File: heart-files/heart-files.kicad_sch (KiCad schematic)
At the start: 31 parts, among them SW10 SW_Push, SW11 SW_Push, SW12 SW_Push, SW13 SW_Push, SW14 SW_Push, SW15 SW_Push, SW16 SW_Push, SW2 SW_Push, SW3 SW_Push, SW4 SW_Push, SW5 SW_Push, SW6 SW_Push, SW7 SW_Push, SW8 SW_Push, SW9 SW_Push

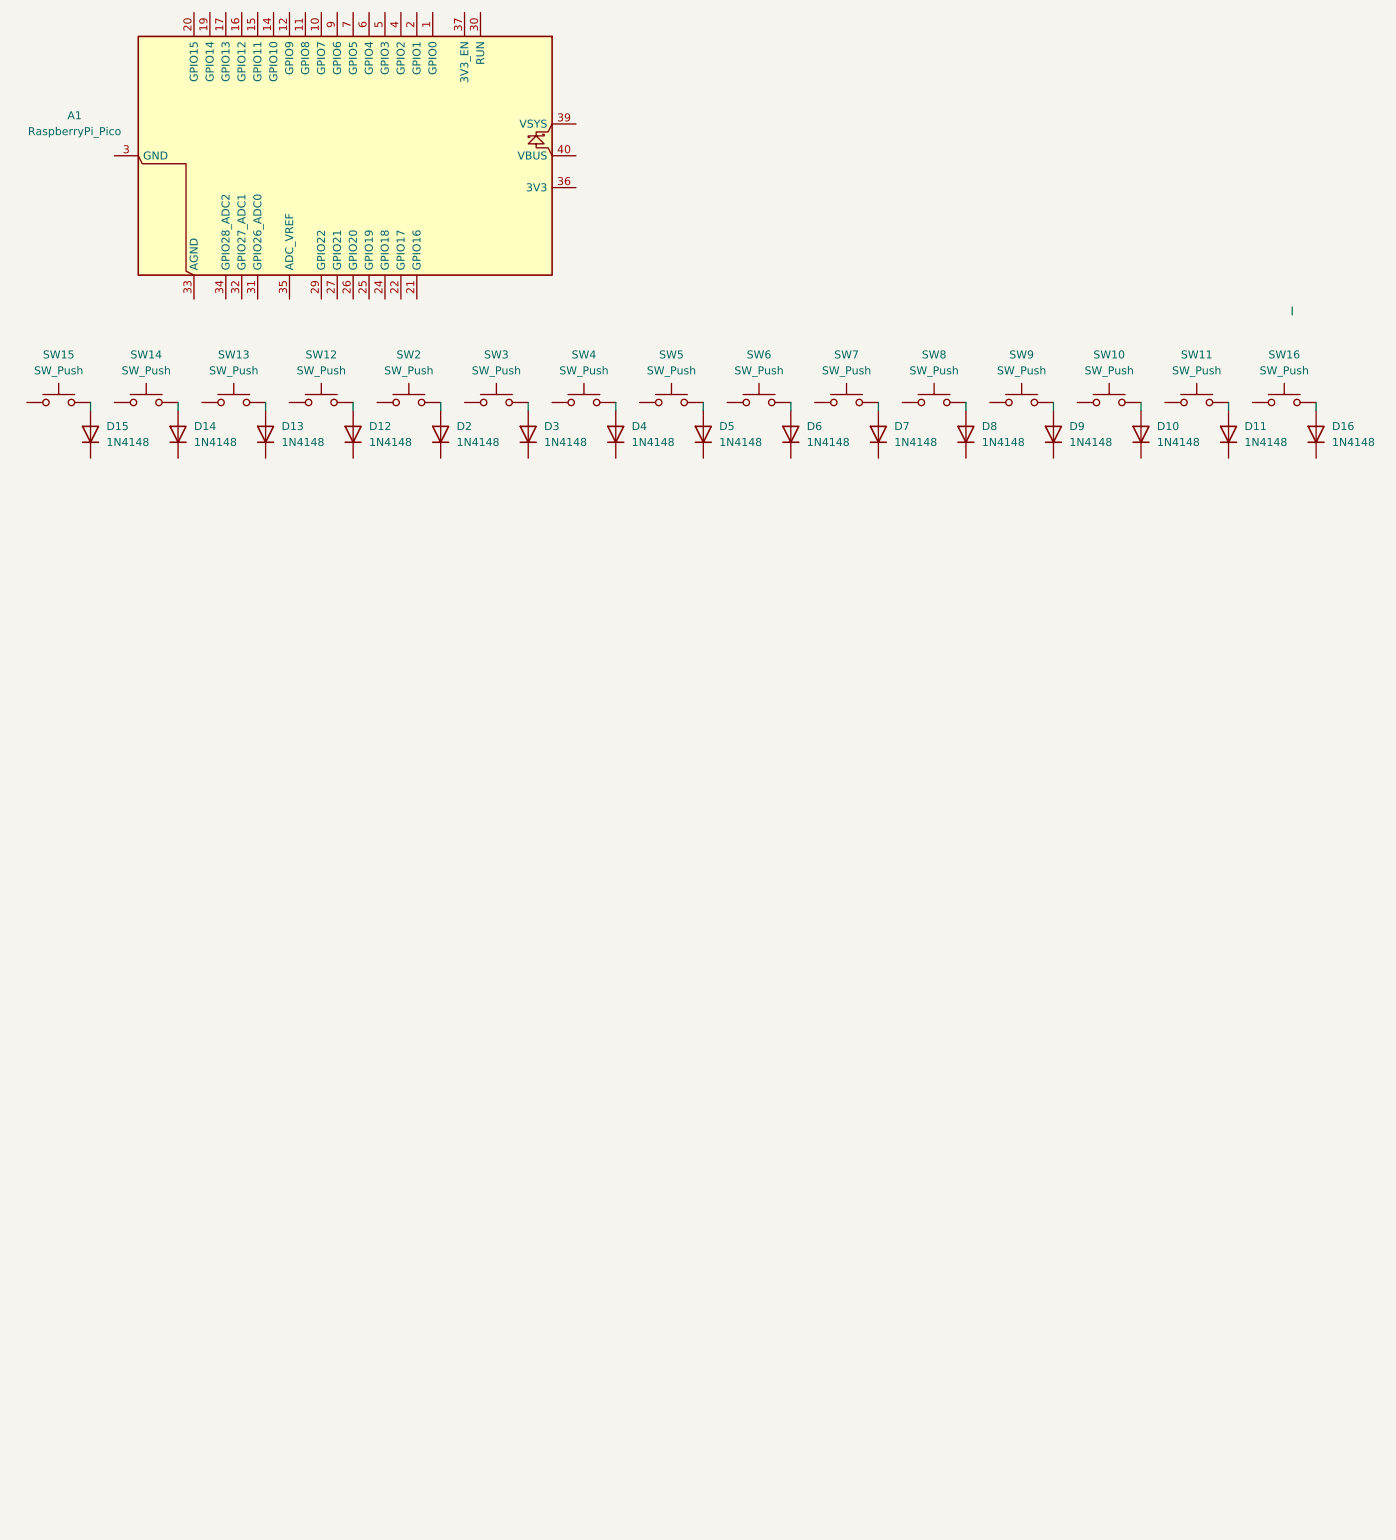
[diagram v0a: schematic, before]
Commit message: update readme and develop pcb, init bom(b)
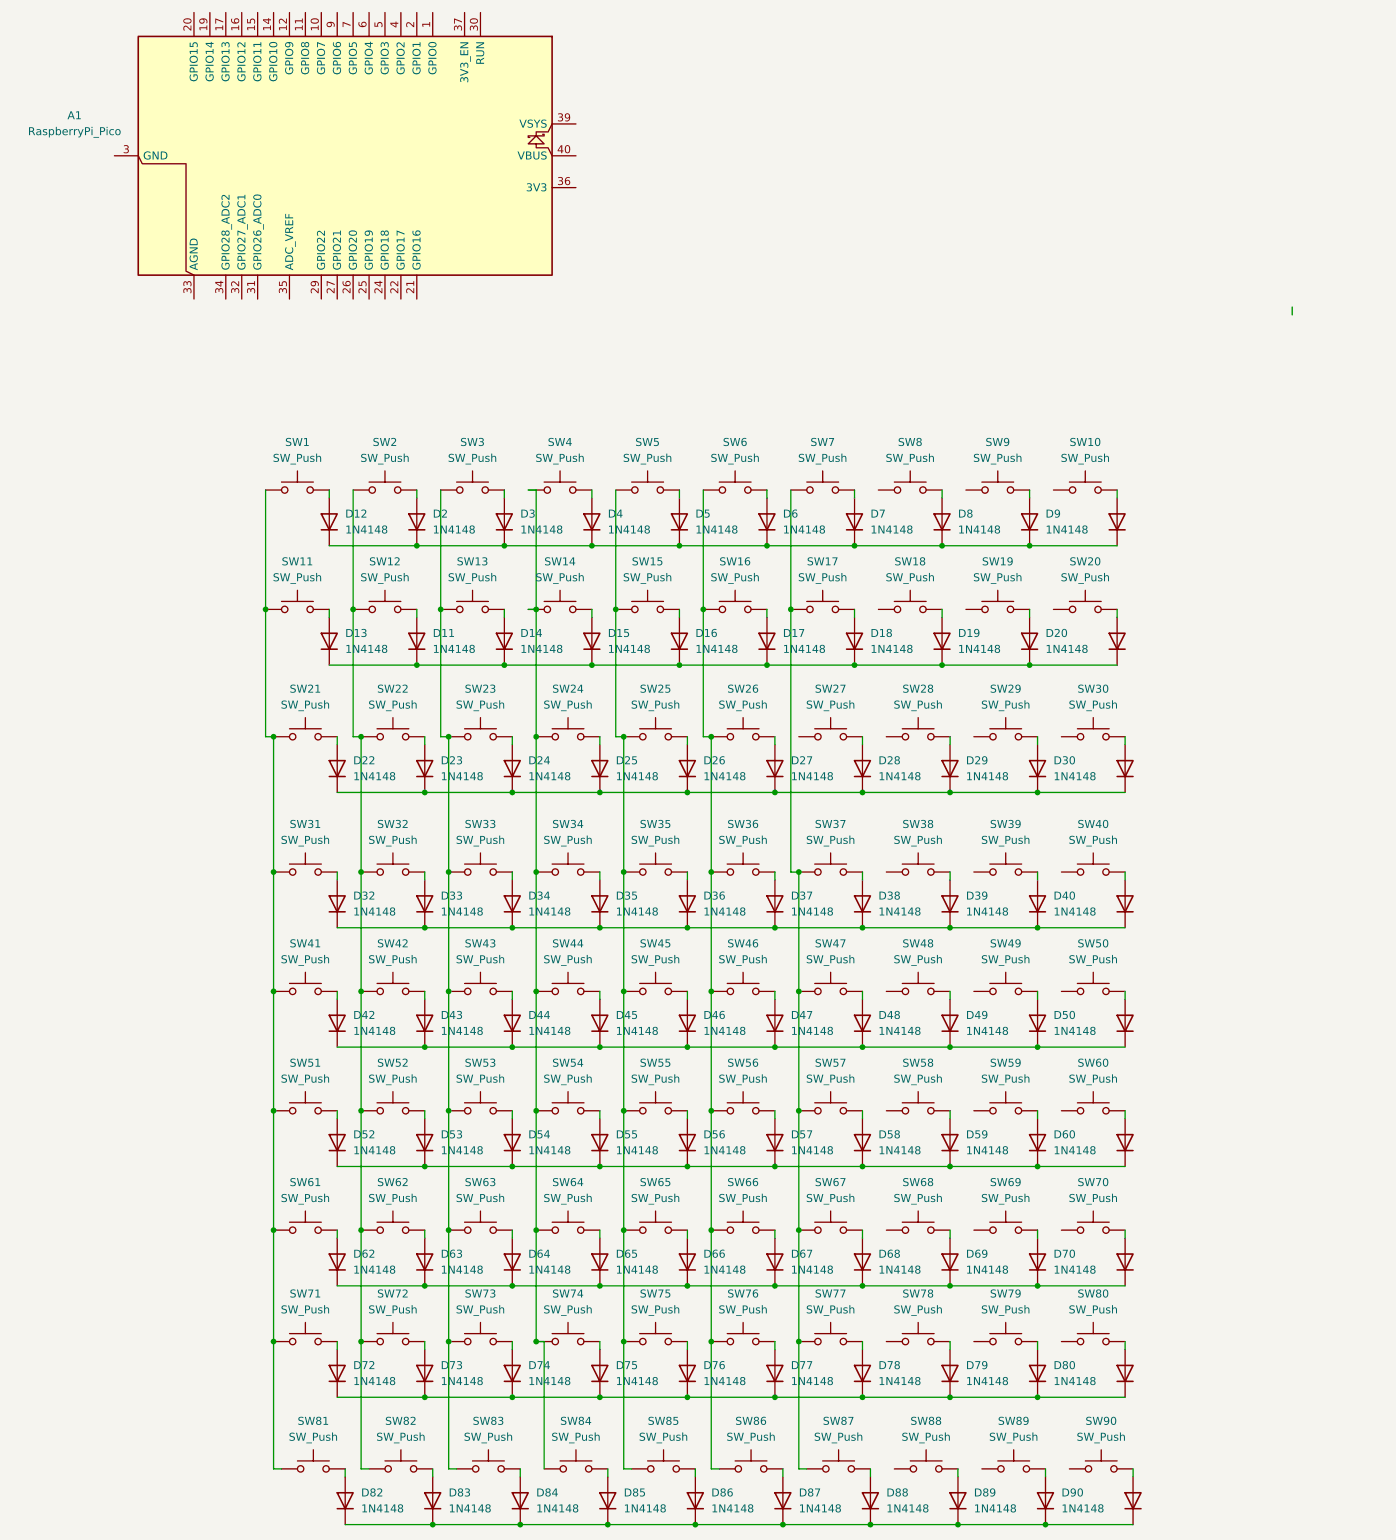
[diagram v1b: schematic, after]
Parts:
- added D17, D18, D19, D20, D21, D22, D23, D24, D25, D26, D27, D28, D29, D30, D31, D32, D33, D34, D35, D36, D37, D38, D39, D40, D41, D42, D43, D44, D45, D46, D47, D48, D49, D50, D51, D52, D53, D54, D55, D56, D57, D58, D59, D60, D61, D62, D63, D64, D65, D66, D67, D68, D69, D70, D71, D72, D73, D74, D75, D76, D77, D78, D79, D80, D81, D82, D83, D84, D85, D86, D87, D88, D89, D90, D91: 1N4148, Diode_THT:D_DO-35_SOD27_P7.62mm_Horizontal, symbol Diode:1N4148
- added SW12, SW17, SW18, SW19, SW20, SW21, SW22, SW23, SW24, SW25, SW26, SW27, SW28, SW29, SW30, SW31, SW32, SW33, SW34, SW35, SW36, SW37, SW38, SW39, SW40, SW41, SW42, SW43, SW44, SW45, SW46, SW47, SW48, SW49, SW50, SW51, SW52, SW53, SW54, SW55, SW56, SW57, SW58, SW59, SW60, SW61, SW62, SW63, SW64, SW65, SW66, SW67, SW68, SW69, SW70, SW71, SW72, SW73, SW74, SW75, SW76, SW77, SW78, SW79, SW80, SW81, SW82, SW83, SW84, SW85, SW86, SW87, SW88, SW89, SW90: SW_Push, symbol Switch:SW_Push
- renumbered SW12 to SW1
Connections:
- net at D10.1 (K): now also D12.1 (K), D2.1 (K), D3.1 (K), D4.1 (K), D5.1 (K), D6.1 (K), D7.1 (K), D8.1 (K), D9.1 (K)
- net at D11.1 (K): now also D13.1 (K), D14.1 (K), D15.1 (K), D16.1 (K), D17.1 (K), D18.1 (K), D19.1 (K), D20.1 (K), D21.1 (K)
- net at D11.2 (A): now also SW12.2; no longer SW11.2
- net at SW3.1: now also SW13.1, SW23.1, SW33.1, SW43.1, SW53.1, SW63.1, SW73.1, SW83.1
- net at SW14.1: now also SW4.1, SW24.1, SW34.1, SW44.1, SW54.1, SW64.1, SW74.1, SW84.1
- net at SW14.2: now also D15.2 (A); no longer D14.2 (A)
- net at D13.2 (A): now also SW11.2; no longer SW13.2
- net at D16.2 (A): now also SW15.2; no longer SW16.2
- net at SW11.1: now also SW1.1, SW21.1, SW31.1, SW41.1, SW51.1, SW61.1, SW71.1, SW81.1
- net at SW6.1: now also SW16.1, SW26.1, SW36.1, SW46.1, SW56.1, SW66.1, SW76.1, SW86.1
- net at SW2.1: now also SW12.1, SW22.1, SW32.1, SW42.1, SW52.1, SW62.1, SW72.1, SW82.1
- net at SW15.1: now also SW5.1, SW25.1, SW35.1, SW45.1, SW55.1, SW65.1, SW75.1, SW85.1
- net at SW7.1: now also SW17.1, SW37.1, SW47.1, SW57.1, SW67.1, SW77.1, SW87.1
- new net: D52.1 (K), D53.1 (K), D54.1 (K), D55.1 (K), D56.1 (K), D57.1 (K), D58.1 (K), D59.1 (K), D60.1 (K), D61.1 (K)
- new net: D60.2 (A), SW59.2
- new net: D32.1 (K), D33.1 (K), D34.1 (K), D35.1 (K), D36.1 (K), D37.1 (K), D38.1 (K), D39.1 (K), D40.1 (K), D41.1 (K)
- new net: D32.2 (A), SW31.2
- new net: D53.2 (A), SW52.2
- new net: D50.2 (A), SW49.2
- new net: D42.1 (K), D43.1 (K), D44.1 (K), D45.1 (K), D46.1 (K), D47.1 (K), D48.1 (K), D49.1 (K), D50.1 (K), D51.1 (K)
- new net: D45.2 (A), SW44.2
- new net: D74.2 (A), SW73.2
- new net: D82.2 (A), SW81.2
- new net: D25.2 (A), SW24.2
- new net: D72.1 (K), D73.1 (K), D74.1 (K), D75.1 (K), D76.1 (K), D77.1 (K), D78.1 (K), D79.1 (K), D80.1 (K), D81.1 (K)
- new net: D81.2 (A), SW80.2
- new net: D80.2 (A), SW79.2
- new net: D64.2 (A), SW63.2
- new net: D33.2 (A), SW32.2
- new net: D37.2 (A), SW36.2
- new net: D77.2 (A), SW76.2
- new net: D43.2 (A), SW42.2
- new net: D57.2 (A), SW56.2
- new net: D44.2 (A), SW43.2
- new net: D19.2 (A), SW18.2
- new net: D34.2 (A), SW33.2
- new net: D41.2 (A), SW40.2
- new net: D82.1 (K), D83.1 (K), D84.1 (K), D85.1 (K), D86.1 (K), D87.1 (K), D88.1 (K), D89.1 (K), D90.1 (K), D91.1 (K)
- new net: D87.2 (A), SW86.2
- new net: D46.2 (A), SW45.2
- new net: D62.1 (K), D63.1 (K), D64.1 (K), D65.1 (K), D66.1 (K), D67.1 (K), D68.1 (K), D69.1 (K), D70.1 (K), D71.1 (K)
- new net: D71.2 (A), SW70.2
- new net: D27.2 (A), SW26.2
- new net: D48.2 (A), SW47.2
- new net: D85.2 (A), SW84.2
- new net: D75.2 (A), SW74.2
- new net: D52.2 (A), SW51.2
- new net: D79.2 (A), SW78.2
- new net: D63.2 (A), SW62.2
- new net: D22.1 (K), D23.1 (K), D24.1 (K), D25.1 (K), D26.1 (K), D27.1 (K), D28.1 (K), D29.1 (K), D30.1 (K), D31.1 (K)
- new net: D23.2 (A), SW22.2
- new net: D22.2 (A), SW21.2
- new net: D69.2 (A), SW68.2
- new net: D47.2 (A), SW46.2
- new net: D17.2 (A), SW16.2
- new net: D20.2 (A), SW19.2
- new net: D40.2 (A), SW39.2
- new net: D55.2 (A), SW54.2
- new net: D54.2 (A), SW53.2
- new net: D42.2 (A), SW41.2
- new net: D67.2 (A), SW66.2
- new net: D59.2 (A), SW58.2
- new net: D90.2 (A), SW89.2
- new net: D61.2 (A), SW60.2
- new net: D73.2 (A), SW72.2
- new net: D76.2 (A), SW75.2
- new net: D39.2 (A), SW38.2
- new net: D49.2 (A), SW48.2
- new net: D70.2 (A), SW69.2
- new net: D38.2 (A), SW37.2
- new net: D89.2 (A), SW88.2
- new net: D84.2 (A), SW83.2
- new net: D83.2 (A), SW82.2
- new net: D68.2 (A), SW67.2
- new net: D26.2 (A), SW25.2
- new net: D86.2 (A), SW85.2
- new net: D51.2 (A), SW50.2
- new net: D62.2 (A), SW61.2
- new net: D66.2 (A), SW65.2
- new net: D36.2 (A), SW35.2
- new net: D31.2 (A), SW30.2
- new net: D30.2 (A), SW29.2
- new net: D91.2 (A), SW90.2
- new net: D29.2 (A), SW28.2
- new net: D72.2 (A), SW71.2
- new net: D21.2 (A), SW20.2
- new net: D65.2 (A), SW64.2
- new net: D14.2 (A), SW13.2
- new net: D58.2 (A), SW57.2
- new net: D24.2 (A), SW23.2
- new net: D78.2 (A), SW77.2
- new net: D56.2 (A), SW55.2
- new net: D88.2 (A), SW87.2
- new net: D35.2 (A), SW34.2
- new net: D18.2 (A), SW17.2
- new net: D28.2 (A), SW27.2
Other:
- moved on the sheet: D12, D2, D3, D4, D5, D6, D7, D8, D9, SW1, SW10, SW2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
